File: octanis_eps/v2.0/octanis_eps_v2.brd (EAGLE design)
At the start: 80 x 50 mm, 186 parts, among them Q1 CSD16327Q3_DQG_8, Q2 CSD16327Q3_DQG_8, Q3 CSD16327Q3_DQG_8, Q4 BSS123, Q5 CSD16327Q3_DQG_8, Q6 CSD16327Q3_DQG_8, Q7 BSC0901NS, U1 MSP430FR5969, U10 INA213, U11 MIC5019, U12 TPS61088, U13 TPS61232, U15 Value, U16 Value, U17 Value, U2 OPA2333DGK, U3 TPS2022D, U4 TPS2022D, U5 BQ24650_RVA_16, U7 TPS61232, U9 INA213, X1 32.768kHz

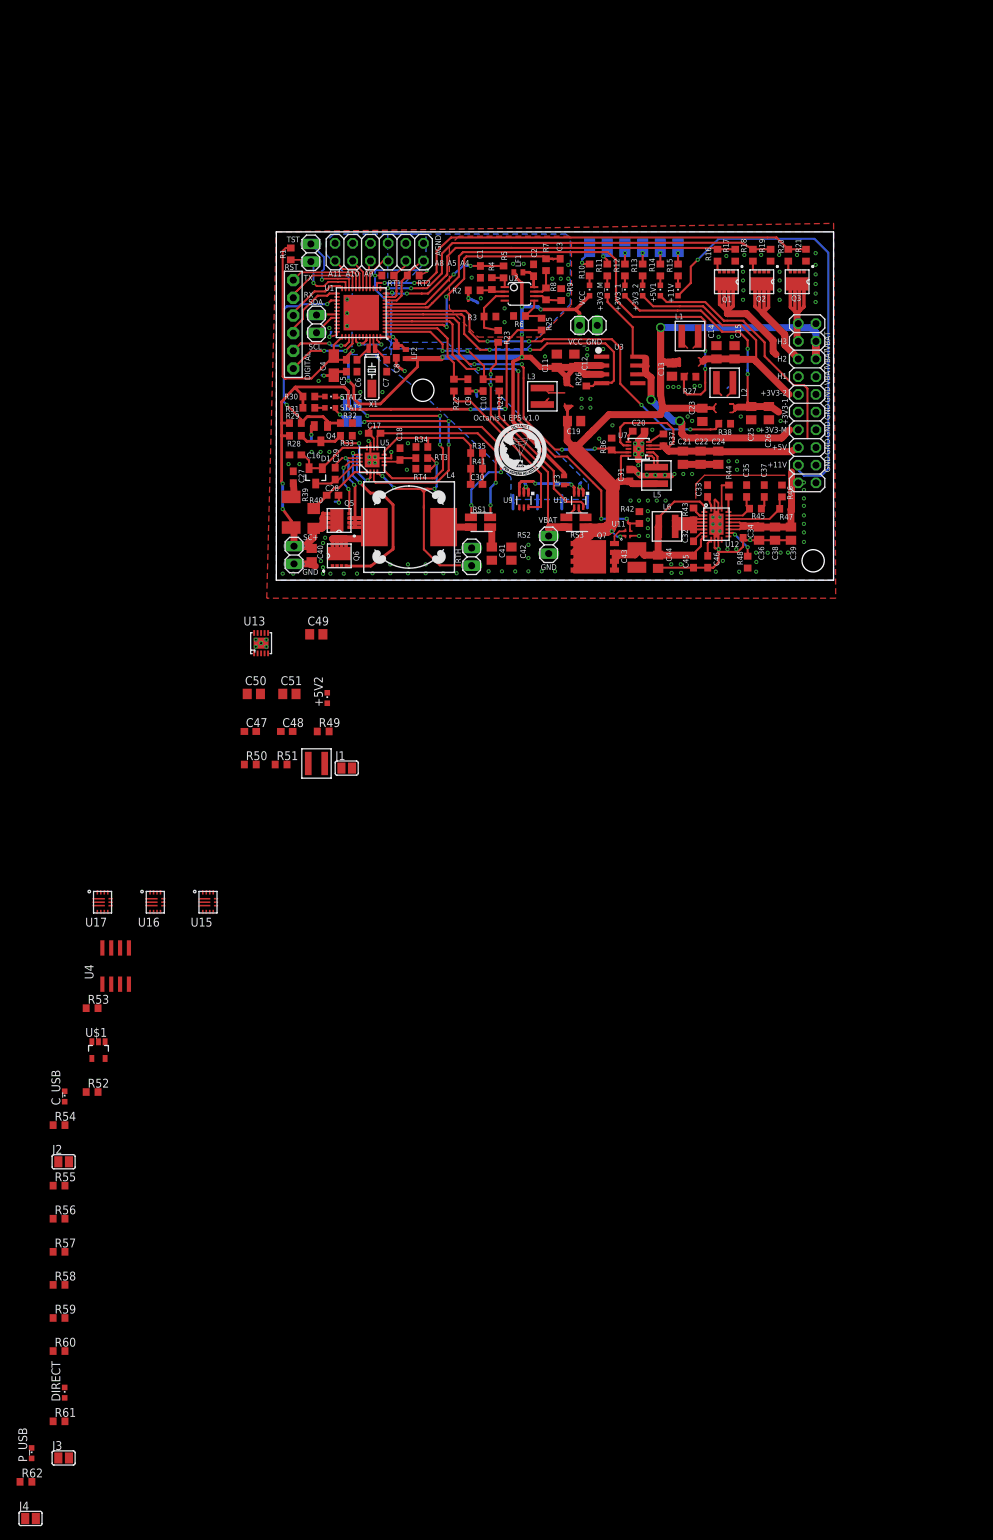
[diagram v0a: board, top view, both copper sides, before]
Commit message: EPS v2.0 finished routing
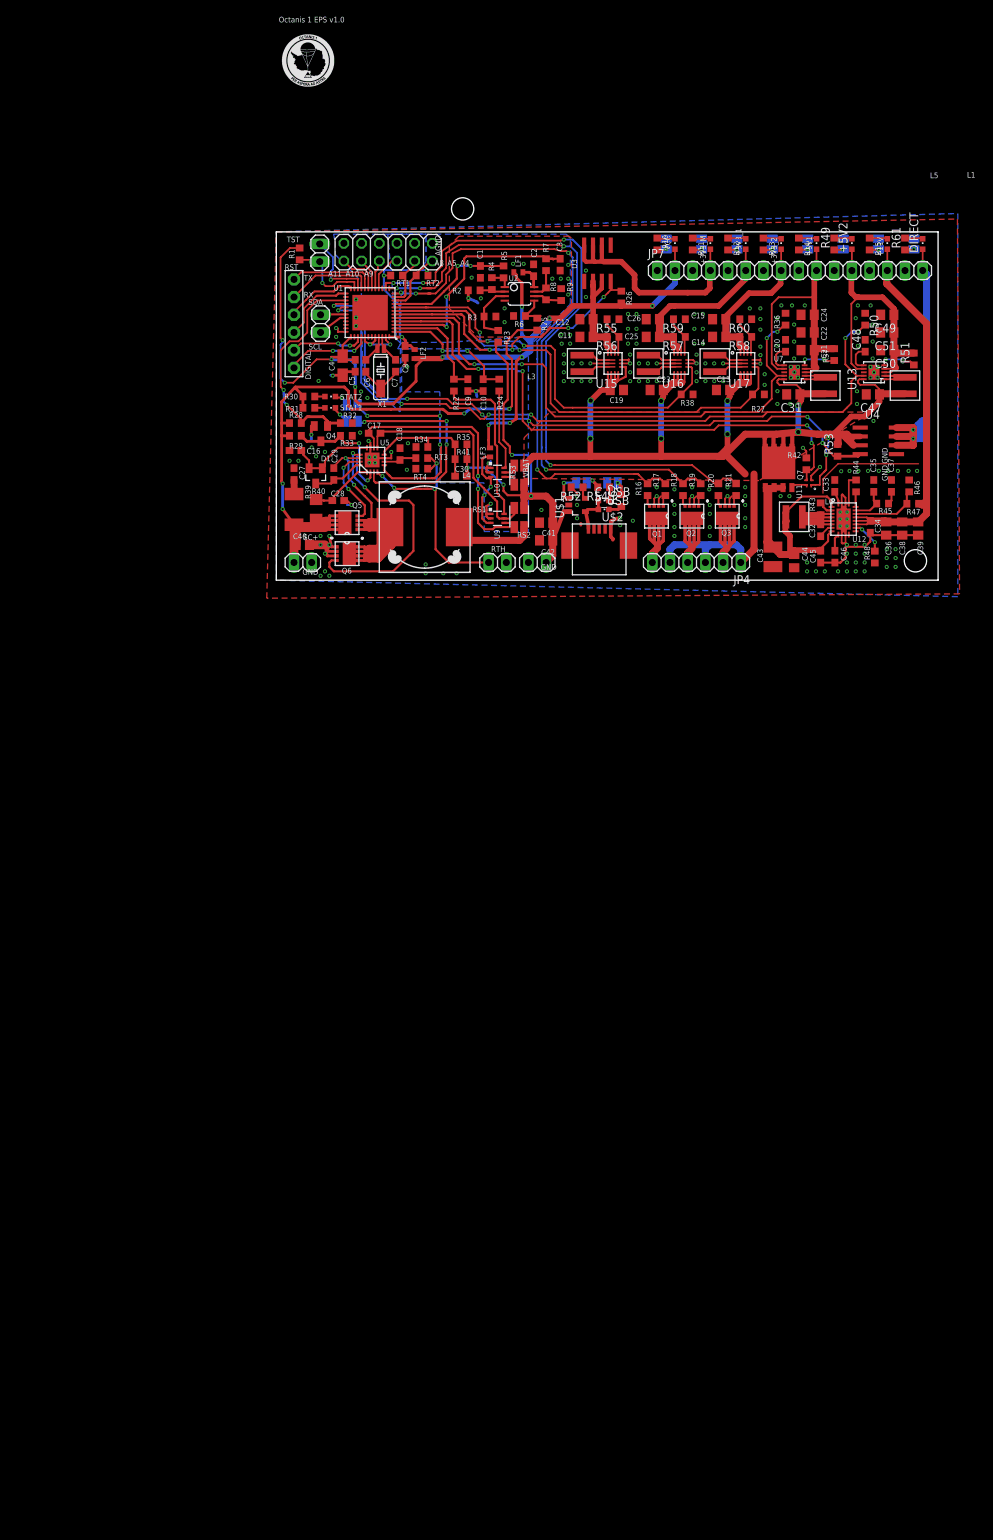
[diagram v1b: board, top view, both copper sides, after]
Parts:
- removed VCC_GND: (no value), Headerlibrary:1X02
- added JP7: (no value), Headerlibrary:1X16
- added U$2: UX60SC-MB-5ST, usbminib:UX60SC-MB-5ST
- C31, C47: device rcl:C0603 -> resistor:C0805
- JP4: device pinhead:2X10 -> Headerlibrary:1X06
- moved J3 212.8 mm to (91.5, 48.3), flipped to the bottom, turned to 270 degrees
- moved R61 208.1 mm to (90.2, 48.3), turned to 90 degrees
- moved DIRECT 205.8 mm to (92.8, 48.3)
- moved R60 177.9 mm to (67.4, 37.5), turned to 180 degrees
- moved J4 170.5 mm to (48.3, 14.0), flipped to the bottom
- moved R59 168.8 mm to (57.9, 37.5), turned to 180 degrees
- moved R58 168.0 mm to (67.4, 34.9), turned to 180 degrees
- moved R62 164.8 mm to (49.5, 11.4), turned to 90 degrees
- moved R57 158.7 mm to (57.9, 34.9), turned to 180 degrees
- moved P_USB 158.4 mm to (47.0, 10.2), turned to 270 degrees
- moved R56 149.5 mm to (48.3, 34.9), turned to 180 degrees
- moved R55 147.6 mm to (48.3, 37.5), turned to 180 degrees
- moved R53 133.7 mm to (80.6, 18.6), turned to 90 degrees
- moved U4 132.9 mm to (86.4, 20.0), turned to 270 degrees
- moved J2 122.6 mm to (43.8, 14.0), flipped to the bottom, turned to 180 degrees
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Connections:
- net +12V: now also JP7.14; no longer JP4.4
- net +3V3: now also JP7.2; no longer VCC_GND.1
- net +3V3_1: now also JP7.6; no longer JP4.12
- net +3V3_2: now also JP7.8; no longer JP4.14
- net +3V3_M: now also JP7.4; no longer JP4.10
- net +5V_1: now also JP7.10; no longer JP4.6
- net +5V_2: now also JP7.12; no longer JP4.8
- net BAT_OUT: now also JP4.1, JP4.3, JP4.5; no longer JP4.15, JP4.17, JP4.19
- net DIRECT: now also JP7.16; no longer JP4.2
- net GND: now also JP7.1, JP7.11, JP7.13, JP7.15, JP7.3, JP7.5, JP7.7, JP7.9, U$2.5; no longer JP4.1, JP4.11, JP4.13, JP4.3, JP4.5, JP4.7, JP4.9, VCC_GND.2
- net HEAT1: now also JP4.6; no longer JP4.16
- net HEAT2: now also JP4.4; no longer JP4.18
- net HEAT3: now also JP4.2; no longer JP4.20
- net V_USB: now also U$2.1
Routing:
- net EN_5V_2: track 0.00 -> 103.9 mm, vias 0 -> 6
- net EN_DIRECT: track 0.00 -> 94.5 mm, vias 0 -> 6
- net BAT_OUT: track 134.6 -> 211.2 mm, vias 3 -> 10
- net DIRECT: track 0.00 -> 45.6 mm, vias 0 -> 2
- net +5V_2: track 0.00 -> 41.8 mm
- net +5V_1: track 74.3 -> 43.5 mm
- net EN_HEAT1: track 54.7 -> 84.7 mm, vias 2 -> 4
- net EN_5V_1: track 51.8 -> 81.1 mm
- net EN_HEAT2: track 60.6 -> 89.7 mm, vias 2 -> 4
- net +12V: track 85.4 -> 57.2 mm, vias 1 -> 0
- net EN_HEAT3: track 67.5 -> 95.5 mm, vias 2 -> 4
- net BAT+: track 41.6 -> 65.2 mm, vias 2 -> 4
- net EN_12V: track 58.9 -> 82.0 mm
- net GND: track 90.4 -> 112.4 mm, vias 137 -> 175
- net +3V3_2: track 39.1 -> 25.3 mm
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- added copper zone on layer 1, net BAT_OUT
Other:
- board size 80 x 50 mm -> 95 x 50 mm
- board text removed: "+11V"
- board text removed: "+3V3-1"
- board text removed: "+3V3-2"
- board text removed: "+3V3-M"
- board text removed: "+5V"
- board text removed: "H1"
- board text removed: "H2"
- board text removed: "H3"
- board text removed: "L2"

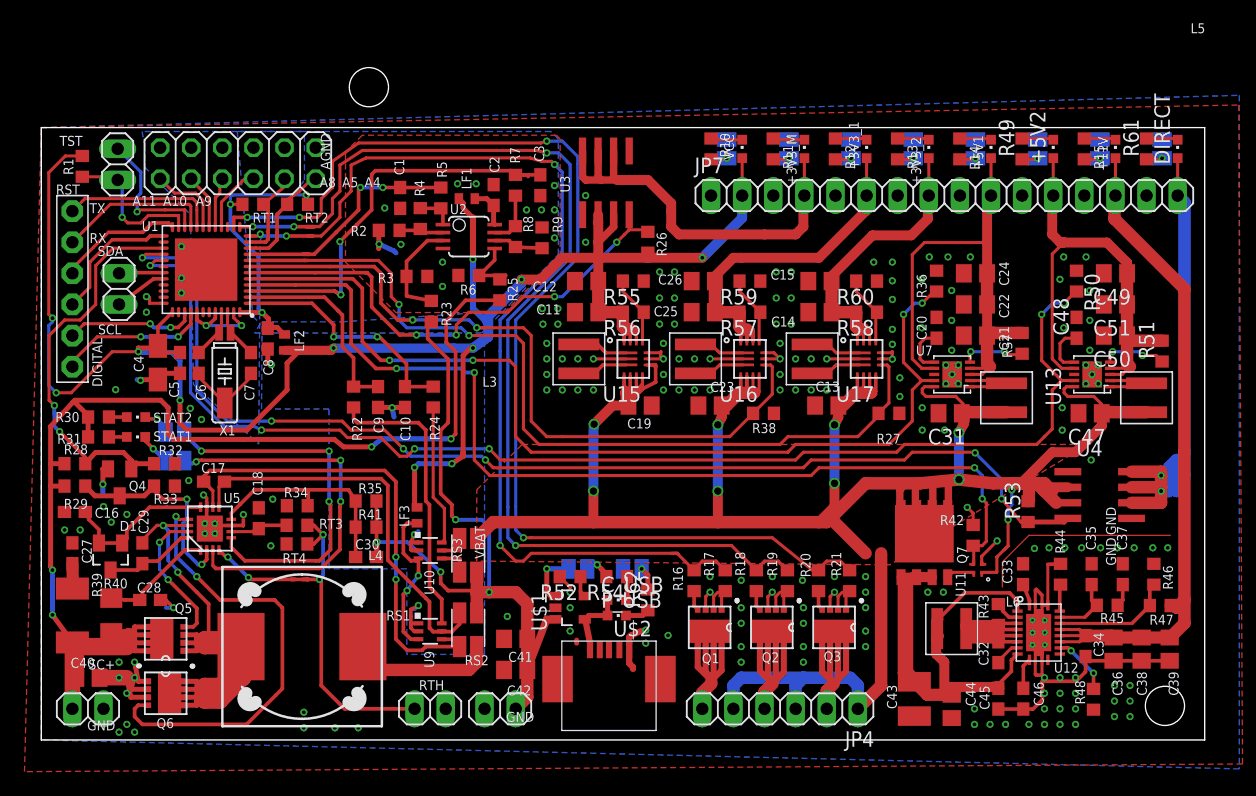
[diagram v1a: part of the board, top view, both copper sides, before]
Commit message: performed DRC
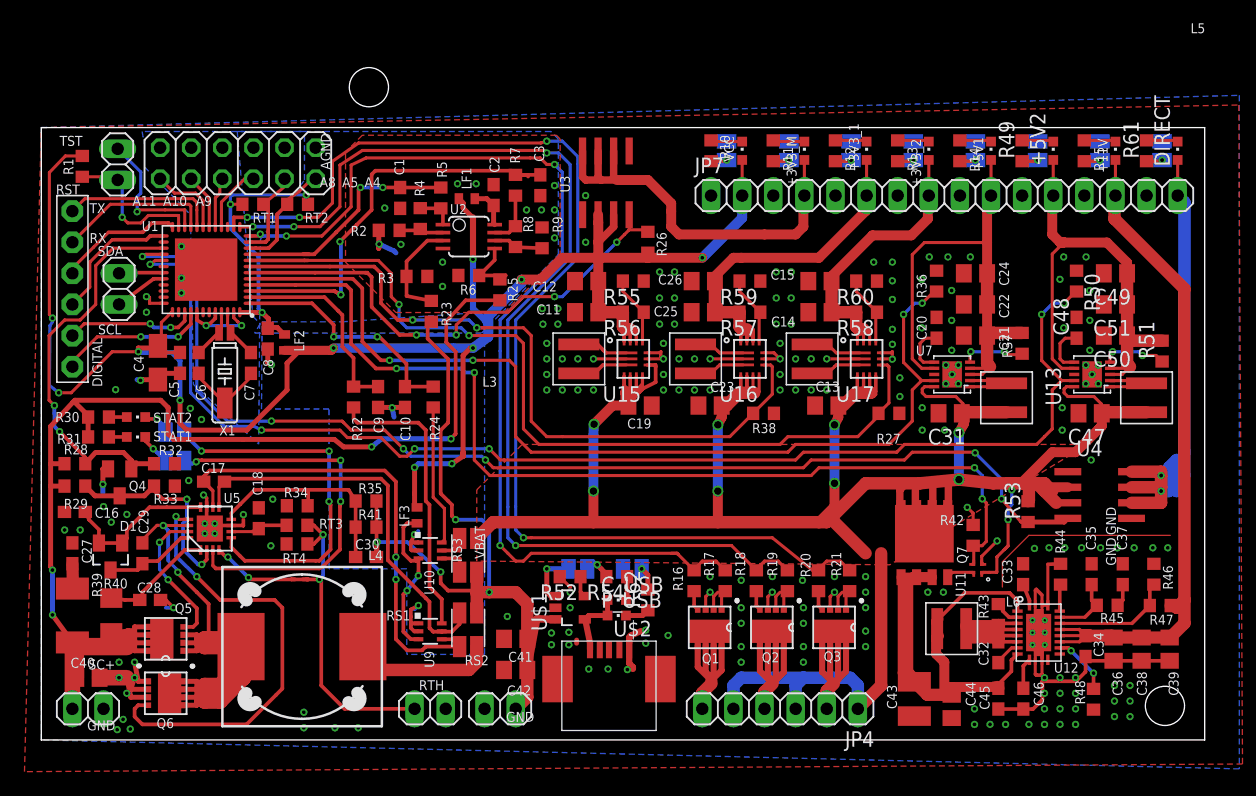
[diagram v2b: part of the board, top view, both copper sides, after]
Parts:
- moved +11V 0.15 mm to (87.7, 48.1)
- moved +3V3_1 0.15 mm to (67.4, 48.1)
- moved +3V3_2 0.15 mm to (72.5, 48.1)
- moved +3V3_M 0.15 mm to (62.3, 48.1)
- moved +5V1 0.15 mm to (77.5, 48.1)
- moved +5V2 0.15 mm to (82.6, 48.1)
- moved DIRECT 0.15 mm to (92.8, 48.1)
- moved J1 0.15 mm to (81.4, 48.1)
- moved J102 0.15 mm to (86.4, 48.1)
- moved J103 0.15 mm to (76.3, 48.1)
- moved J104 0.15 mm to (71.2, 48.1)
- moved J105 0.15 mm to (66.1, 48.1)
- moved J106 0.15 mm to (61.0, 48.1)
- moved J107 0.15 mm to (56.0, 48.1)
- moved J3 0.15 mm to (91.5, 48.1)
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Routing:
- net BAT_OUT: track 211.2 -> 230.4 mm
- net BAT_OUT1: track 11.8 -> 0.00 mm
- net +3V3_3: track 10.5 -> 0.00 mm
- net +3V3_1: track 30.2 -> 40.5 mm
- net +3V3_4: track 10.1 -> 0.00 mm
- net +3V3: track 158.9 -> 168.8 mm
- net BAT_OUT2: track 7.35 -> 0.00 mm
- net BAT+: track 65.2 -> 65.8 mm
- net EN_HEAT2: track 89.7 -> 89.1 mm
- net GND: vias 175 -> 181
